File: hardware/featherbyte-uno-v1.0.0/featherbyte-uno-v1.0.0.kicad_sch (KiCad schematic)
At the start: 35 parts, among them J1 Conn_01x08, J2 Conn_01x10, J3 Conn_01x06, J4 Conn_01x08, J5 USB_C_16P, J7 Screw_Terminal_01x02, J8 USB_C_Receptacle_16P, U1 CH32V203CxT6, U4 AMS1117-3.3, U5 USBLC6-2P6, U6 USBLC6-2P6, Y1 8M, Y3 32.768K

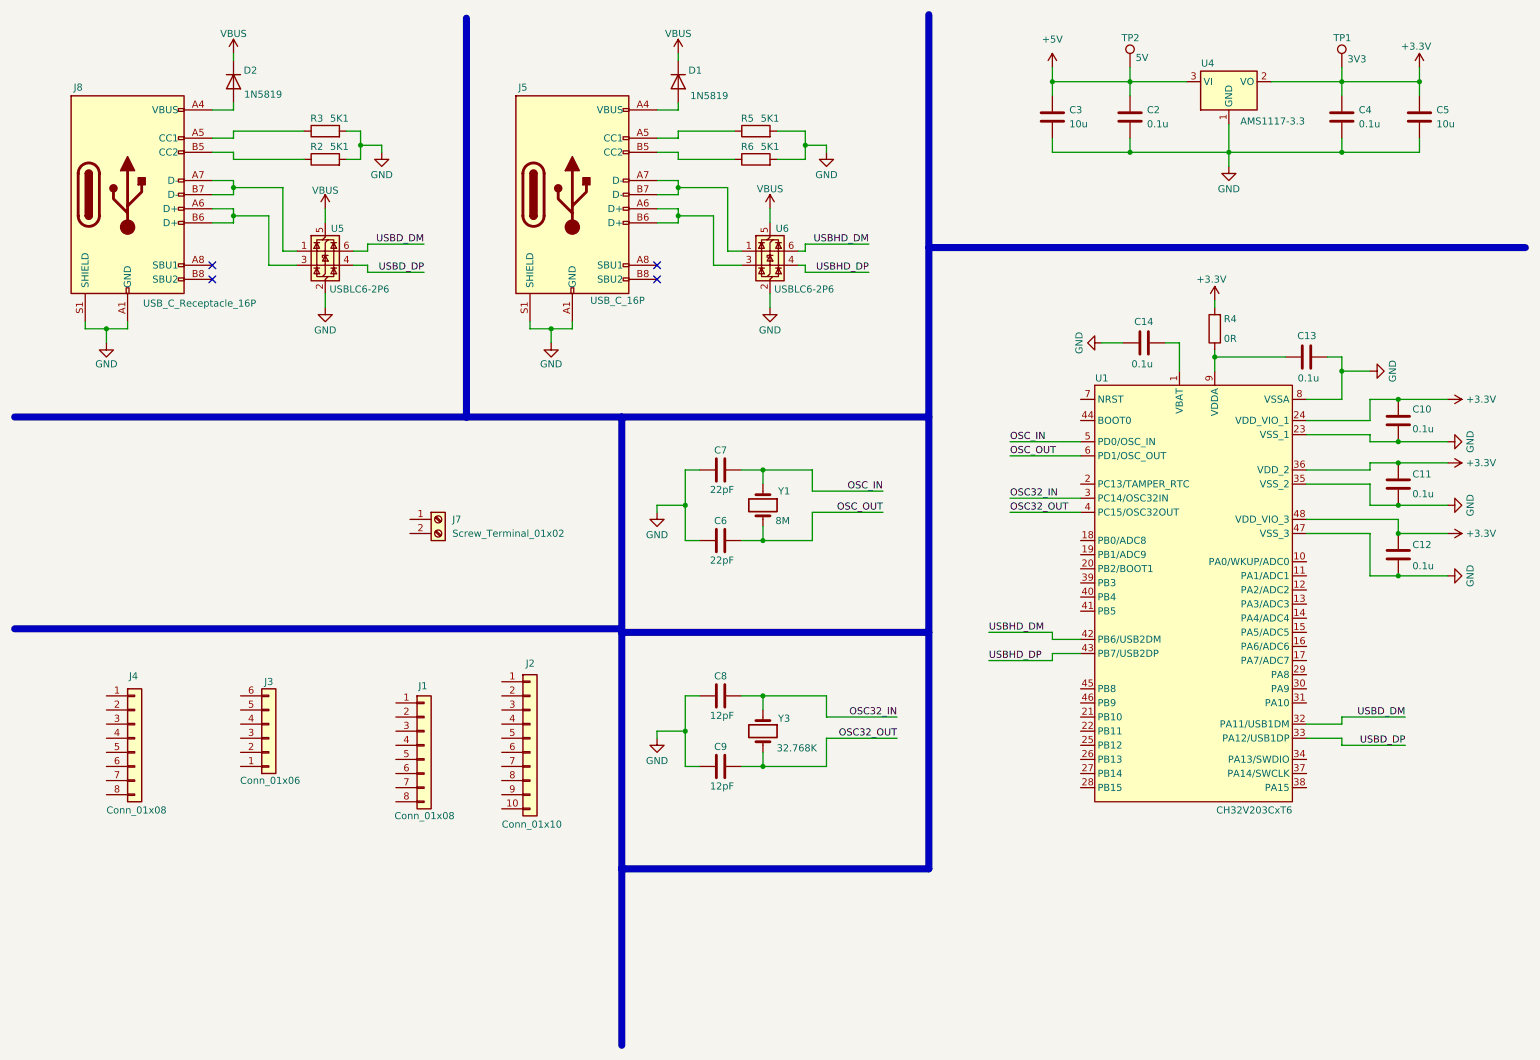
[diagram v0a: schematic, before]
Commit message: canbus, and programing circuitry added
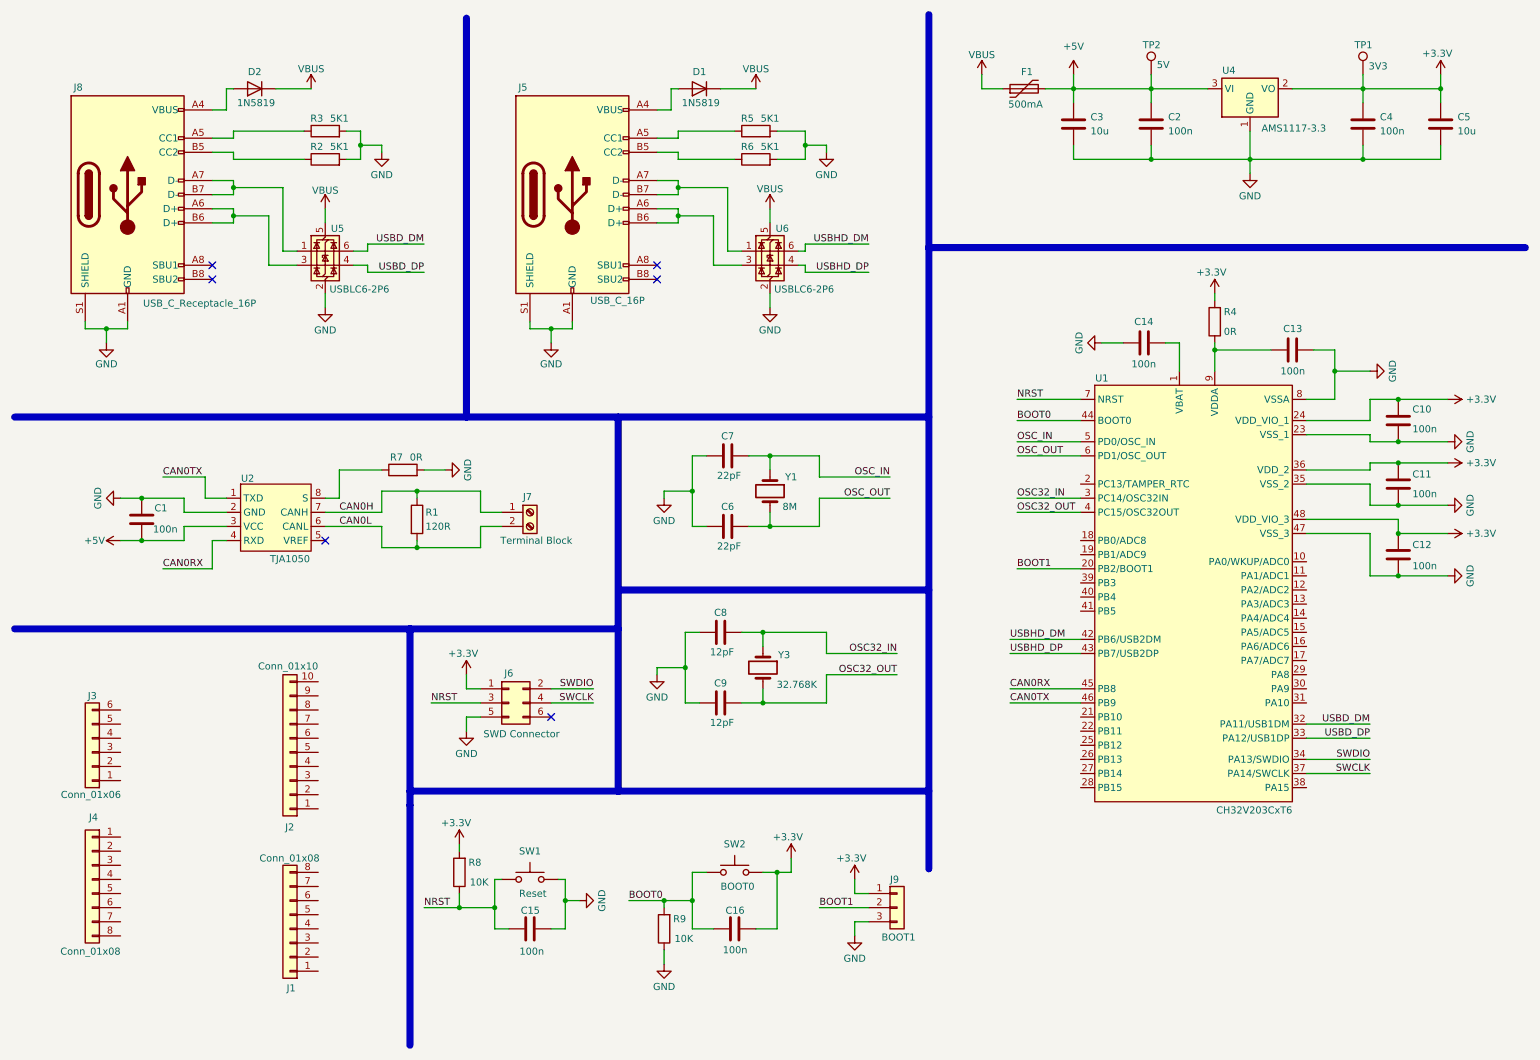
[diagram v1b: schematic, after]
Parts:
- added C1, C15, C16: 100n, symbol Device:C
- added F1: 500mA, symbol Device:Polyfuse
- added J6: SWD Connector, symbol Connector_Generic:Conn_02x03_Odd_Even
- added J9: BOOT1, symbol Connector_Generic:Conn_01x03
- added R1: 120R, symbol Device:R
- added R7: 0R, symbol Device:R
- added R8, R9: 10K, symbol Device:R
- added SW1: Reset, symbol Switch:SW_Push
- added SW2: BOOT0, symbol Switch:SW_Push
- added U2: TJA1050, symbol TJA1050:TJA1050
- C10, C11, C12, C13, C14, C2, C4: value 0.1u -> 100n
- J7: value Screw_Terminal_01x02 -> Terminal Block
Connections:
- net +3.3V: now also C16.2, J6.1 (Pin_1), J9.1 (Pin_1), R8.2, SW2.2
- net +5V: now also C1.2, F1.2, U2.3 (VCC)
- net GND: now also C1.1, C15.2, J6.5 (Pin_5), J9.3 (Pin_3), R7.2, R9.1, SW1.2, U2.2 (GND)
- net VBUS: now also F1.1
- net BOOT1: now reaches U1.20 (PB2/BOOT1)
- net BOOT1: now also J9.2 (Pin_2)
- net SWDIO: now reaches U1.34 (PA13/SWDIO)
- net SWDIO: now also J6.2 (Pin_2)
- net SWCLK: now reaches U1.37 (PA14/SWCLK)
- net SWCLK: now also J6.4 (Pin_4)
- net BOOT0: now reaches U1.44 (BOOT0)
- net BOOT0: now also C16.1, R9.2, SW2.1
- net CAN0RX: now reaches U1.45 (PB8)
- net CAN0RX: now also U2.4 (RXD)
- net CAN0TX: now reaches U1.46 (PB9)
- net CAN0TX: now also U2.1 (TXD)
- net NRST: now reaches U1.7 (NRST)
- net NRST: now also C15.1, J6.3 (Pin_3), R8.1, SW1.1
- net CAN0H: now reaches J7.1 (Pin_1)
- net CAN0H: now also R1.1, U2.7 (CANH)
- net CAN0L: now reaches J7.2 (Pin_2)
- net CAN0L: now also R1.2, U2.6 (CANL)
- new net: R7.1, U2.8 (S)
- no-connect marks 4 -> 6
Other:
- moved on the sheet: C13, C2, C3, C4, C5, C6, C7, C8, C9, D2, J1, J2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

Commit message: schematics ready for layout
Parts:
- removed J4: Conn_01x08, symbol Connector_Generic:Conn_01x08
- added C17: 10u, symbol Device:C
- added D3: GREEN, symbol Device:LED
- added D4: YELLOW, symbol Device:LED
- added J10: Conn_01x09, symbol Connector_Generic:Conn_01x09
- added JP1: Jumper, symbol Jumper:SolderJumper_2_Open
- added R10, R11, R12, R15, R16: 0R, symbol Device:R
- added R13, R14: 1K, symbol Device:R
- added SW3: SW_DIP_x04, symbol Switch:SW_DIP_x04
- J5: value USB_C_16P -> USB_C_Receptacle_16P
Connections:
- net +3.3V: now also J10.5 (Pin_5), J10.7 (Pin_7), J10.8 (Pin_8), J10.9 (Pin_9), R10.2, R13.1
- net +5V: now also C17.1, J10.1 (Pin_1), J10.4 (Pin_4)
- net CAN0H: now also JP1.2 (B); no longer R1.1
- net GND: now also J2.4 (Pin_4), C17.2, D3.1 (K), D4.1 (K), J10.2 (Pin_2), J10.3 (Pin_3)
- net NRST: now also J10.6 (Pin_6)
- net VBUS: now also R15.2, R16.2
- net SCL: now reaches J2.1 (Pin_1)
- net SCL: now also U1.21 (PB10), R12.2
- net D8: now reaches J2.10 (Pin_10)
- net D8: now also U1.27 (PB14)
- net SDA: now reaches J2.2 (Pin_2)
- net SDA: now also U1.22 (PB11), R11.2
- net VREF: now reaches J2.3 (Pin_3)
- net VREF: now also C13.1, R4.1, U1.9 (VDDA)
- net D13: now reaches J2.5 (Pin_5)
- net D13: now also U1.39 (PB3)
- net D12: now reaches J2.6 (Pin_6)
- net D12: now also U1.40 (PB4)
- net D11: now reaches J2.7 (Pin_7)
- net D11: now also U1.41 (PB5)
- net D10: now reaches J2.8 (Pin_8)
- net D10: now also U1.38 (PA15)
- net D9: now reaches J2.9 (Pin_9)
- net D9: now also U1.28 (PB15)
- net at J5.A5 (CC1): now also SW3.1, SW3.2; no longer R5.1
- net at J5.B5 (CC2): now also SW3.3, SW3.4; no longer R6.1
- net D0: now reaches J1.1 (Pin_1)
- net D0: now also U1.13 (PA3/ADC3)
- net D1: now reaches J1.2 (Pin_2)
- net D1: now also U1.12 (PA2/ADC2)
- net D2: now reaches J1.3 (Pin_3)
- net D2: now also U1.16 (PA6/ADC6)
- net D3: now reaches J1.4 (Pin_4)
- net D3: now also U1.17 (PA7/ADC7)
- net D4: now reaches J1.5 (Pin_5)
- net D4: now also U1.29 (PA8)
- net D5: now reaches J1.6 (Pin_6)
- net D5: now also U1.30 (PA9)
- net D6: now reaches J1.7 (Pin_7)
- net D6: now also U1.31 (PA10)
- net D7: now reaches J1.8 (Pin_8)
- net D7: now also U1.26 (PB13)
- net A5: now reaches J3.1 (Pin_1)
- net A5: now also U1.19 (PB1/ADC9), R12.1
- net A4: now reaches J3.2 (Pin_2)
- net A4: now also U1.18 (PB0/ADC8), R11.1
- net A3: now reaches J3.3 (Pin_3)
- net A3: now also U1.15 (PA5/ADC5)
- net A2: now reaches J3.4 (Pin_4)
- net A2: now also U1.14 (PA4/ADC4)
- net A1: now reaches J3.5 (Pin_5)
- net A1: now also U1.11 (PA1/ADC1)
- net A0: now reaches J3.6 (Pin_6)
- net A0: now also U1.10 (PA0/WKUP/ADC0)
- net at C14.1, U1.1 (VBAT): now also R10.1
- net LED: now reaches U1.25 (PB12)
- net LED: now also R14.1
- new net: D4.2 (A), R14.2
- new net: JP1.1 (A), R1.1
- new net: D3.2 (A), R13.2
- new net: R15.1, SW3.5
- new net: R6.1, SW3.6
- new net: R5.1, SW3.7
- new net: R16.1, SW3.8
- no-connect marks 6 -> 7
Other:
- moved on the sheet: C1, C13, C14, C16, C2, C3, C4, C5, C6, C7, C8, C9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

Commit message: footprint asignment complete
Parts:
- C1, C10, C11, C12, C13, C14, C15, C16, C2, C4, C6, C7, C8, C9: footprint (none) -> Capacitor_SMD:C_0603_1608Metric
- C17, C3, C5: footprint (none) -> Capacitor_SMD:C_1206_3216Metric
- D1, D2: footprint (none) -> Diode_SMD:D_SOD-123
- D3, D4: footprint (none) -> LED_SMD:LED_0805_2012Metric
- F1: footprint (none) -> Fuse:Fuse_1206_3216Metric
- J1: footprint (none) -> Connector_PinSocket_2.54mm:PinSocket_1x08_P2.54mm_Vertical
- J10: footprint (none) -> Connector_PinSocket_2.54mm:PinSocket_1x09_P2.54mm_Vertical
- J2: footprint (none) -> Connector_PinSocket_2.54mm:PinSocket_1x10_P2.54mm_Vertical
- J3: footprint (none) -> Connector_PinSocket_2.54mm:PinSocket_1x06_P2.54mm_Vertical
- J5, J8: footprint (none) -> Connector_USB:USB_C_Receptacle_HCTL_HC-TYPE-C-16P-01A
- J6: footprint (none) -> Connector_PinHeader_2.54mm:PinHeader_2x03_P2.54mm_Vertical
- J7: footprint (none) -> TerminalBlock:TerminalBlock_MaiXu_MX126-5.0-02P_1x02_P5.00mm
- J9: footprint (none) -> Connector_PinHeader_2.54mm:PinHeader_1x03_P2.54mm_Vertical
- JP1: footprint (none) -> Jumper:SolderJumper-2_P1.3mm_Open_TrianglePad1.0x1.5mm
- R1, R10, R11, R12, R13, R14, R15, R16, R2, R3, R4, R5, R6, R7, R8, R9: footprint (none) -> Resistor_SMD:R_0603_1608Metric
- SW1, SW2: footprint (none) -> Button_Switch_SMD:SW_SPST_CK_RS282G05A3
- SW3: footprint (none) -> Button_Switch_SMD:SW_DIP_SPSTx04_Slide_KingTek_DSHP04TS_W7.62mm_P1.27mm
- TP1, TP2: footprint (none) -> TestPoint:TestPoint_Pad_D1.5mm
- U1: footprint (none) -> Package_QFP:LQFP-48_7x7mm_P0.5mm
- U2: footprint (none) -> Package_SO:SO-8_3.9x4.9mm_P1.27mm
- Y1: footprint (none) -> Crystal:Crystal_SMD_HC49-SD
- Y3: footprint (none) -> Crystal:Crystal_SMD_3215-2Pin_3.2x1.5mm
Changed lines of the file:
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@@
 			)
 		)
-		(property "Footprint" ""
+		(property "Footprint" "Resistor_SMD:R_0603_1608Metric"
 			(at 94.488 165.1 90)
 			(effects
@@
 			)
 		)
-		(property "Footprint" ""
+		(property "Footprint" "Capacitor_SMD:C_0603_1608Metric"
 			(at 262.5852 100.33 0)
 			(effects
@@
 			)
 		)
-		(property "Footprint" ""
+		(property "Footprint" "Crystal:Crystal_SMD_3215-2Pin_3.2x1.5mm"
 			(at 151.13 129.54 0)
 			(effects
@@
 			)
 		)
-		(property "Footprint" ""
+		(property "Footprint" "Resistor_SMD:R_0603_1608Metric"
 			(at 131.318 176.53 90)
 			(effects
@@
 			)
 		)
-		(property "Footprint" ""
+		(property "Footprint" "Connector_PinSocket_2.54mm:PinSocket_1x10_P2.54mm_Vertical"
 			(at 64.77 179.07 0)
 			(effects
@@
 			)
 		)
-		(property "Footprint" ""
+		(property "Footprint" "Capacitor_SMD:C_0603_1608Metric"
 			(at 32.7152 106.68 0)
 			(effects
@@
 			)
 		)
-		(property "Footprint" ""
+		(property "Footprint" "Connector_PinHeader_2.54mm:PinHeader_1x03_P2.54mm_Vertical"
 			(at 171.45 170.18 0)
 			(effects
@@
 			)
 		)
-		(property "Footprint" ""
+		(property "Footprint" "Resistor_SMD:R_0603_1608Metric"
 			(at 69.85 39.878 90)
 			(effects
@@
 			)
 		)
-		(property "Footprint" ""
+		(property "Footprint" "Capacitor_SMD:C_0603_1608Metric"
 			(at 224.4852 35.56 0)
 			(effects
@@
 			)
 		)
-		(property "Footprint" ""
+		(property "Footprint" "Capacitor_SMD:C_1206_3216Metric"
 			(at 272.7452 35.56 0)
 			(effects
@@
 			)
 		)
-		(property "Footprint" ""
+		(property "Footprint" "Diode_SMD:D_SOD-123"
 			(at 57.15 22.86 0)
 			(effects
@@
 			)
 		)
-		(property "Footprint" ""
+		(property "Footprint" "TestPoint:TestPoint_Pad_D1.5mm"
 			(at 228.6 22.86 0)
 			(effects
@@
 			)
 		)
-		(property "Footprint" ""
+		(property "Footprint" "Capacitor_SMD:C_1206_3216Metric"
 			(at 213.0552 35.56 0)
 			(effects
@@
 			)
 		)
-		(property "Footprint" ""
+		(property "Footprint" "Capacitor_SMD:C_0603_1608Metric"
 			(at 139.7 103.8352 0)
 			(effects
@@
 			)
 		)
-		(property "Footprint" ""
+		(property "Footprint" "Resistor_SMD:R_0603_1608Metric"
 			(at 218.948 67.31 90)
 			(effects
@@
 			)
 		)
-		(property "Footprint" ""
+		(property "Footprint" "Capacitor_SMD:C_0603_1608Metric"
 			(at 139.7 136.8552 0)
 			(effects
@@
 			)
 		)
-		(property "Footprint" ""
+		(property "Footprint" "Resistor_SMD:R_0603_1608Metric"
 			(at 29.21 131.318 90)
 			(effects
@@
 			)
 		)
-		(property "Footprint" ""
+		(property "Footprint" "Connector_USB:USB_C_Receptacle_HCTL_HC-TYPE-C-16P-01A"
 			(at 114.3 41.91 0)
 			(effects
@@
 			)
 		)
-		(property "Footprint" ""
+		(property "Footprint" "LED_SMD:LED_0805_2012Metric"
 			(at 64.77 148.59 0)
 			(effects
@@
 			)
 		)
-		(property "Footprint" ""
+		(property "Footprint" "Jumper:SolderJumper-2_P1.3mm_Open_TrianglePad1.0x1.5mm"
 			(at 82.55 100.33 0)
 			(effects
@@
 			)
 		)
-		(property "Footprint" ""
+		(property "Footprint" "Resistor_SMD:R_0603_1608Metric"
 			(at 55.88 150.368 90)
 			(effects
@@
 			)
 		)
-		(property "Footprint" ""
+		(property "Footprint" "Resistor_SMD:R_0603_1608Metric"
 			(at 230.378 67.31 90)
 			(effects
@@
 			)
 		)
-		(property "Footprint" ""
+		(property "Footprint" "Resistor_SMD:R_0603_1608Metric"
 			(at 55.88 137.668 90)
 			(effects
@@
 			)
 		)
-		(property "Footprint" ""
+		(property "Footprint" "Capacitor_SMD:C_0603_1608Metric"
 			(at 139.7 124.1552 0)
 			(effects
@@
 			)
 		)
-		(property "Footprint" ""
+		(property "Footprint" "Capacitor_SMD:C_1206_3216Metric"
 			(at 201.6252 35.56 0)
 			(effects
@@
 			)
 		)
-		(property "Footprint" ""
+		(property "Footprint" "Button_Switch_SMD:SW_DIP_SPSTx04_Slide_KingTek_DSHP04TS_W7.62mm_P1.27mm"
 			(at 146.05 34.29 0)
 			(effects
@@
 			)
 		)
-		(property "Footprint" ""
+		(property "Footprint" "Capacitor_SMD:C_0603_1608Metric"
 			(at 248.92 71.4248 0)
 			(effects
@@
 			)
 		)
-		(property "Footprint" ""
+		(property "Footprint" "Capacitor_SMD:C_0603_1608Metric"
 			(at 262.5852 88.9 0)
 			(effects
@@
 			)
 		)
-		(property "Footprint" ""
+		(property "Footprint" "Crystal:Crystal_SMD_HC49-SD"
 			(at 151.13 96.52 0)
 			(effects
@@
 			)
 		)
-		(property "Footprint" ""
+		(property "Footprint" "Connector_PinHeader_2.54mm:PinHeader_2x03_P2.54mm_Vertical"
 			(at 101.6 134.62 0)
 			(effects
@@
 			)
 		)
-		(property "Footprint" ""
+		(property "Footprint" "Connector_PinSocket_2.54mm:PinSocket_1x09_P2.54mm_Vertical"
 			(at 21.59 154.94 0)
 			(effects
@@
 			)
 		)
-		(property "Footprint" ""
+		(property "Footprint" "Package_SO:SO-8_3.9x4.9mm_P1.27mm"
 			(at 49.53 96.52 0)
 			(effects
@@
 			)
 		)
-		(property "Footprint" ""
+		(property "Footprint" "Resistor_SMD:R_0603_1608Metric"
 			(at 69.85 32.258 90)
 			(effects
@@
 			)
 		)
-		(property "Footprint" ""
+		(property "Footprint" "Button_Switch_SMD:SW_SPST_CK_RS282G05A3"
 			(at 105.41 162.56 0)
 			(effects
@@
 			)
 		)
-		(property "Footprint" ""
+		(property "Footprint" "LED_SMD:LED_0805_2012Metric"
 			(at 64.77 135.89 0)
 			(effects
@@
 			)
 		)
-		(property "Footprint" ""
+		(property "Footprint" "Connector_USB:USB_C_Receptacle_HCTL_HC-TYPE-C-16P-01A"
 			(at 38.1 43.18 0)
 			(effects
@@
 			)
 		)
-		(property "Footprint" ""
+		(property "Footprint" "Resistor_SMD:R_0603_1608Metric"
 			(at 161.29 46.228 90)
 			(effects
@@
 			)
 		)
-		(property "Footprint" ""
+		(property "Footprint" "Resistor_SMD:R_0603_1608Metric"
 			(at 29.21 137.668 90)
 			(effects
@@
 			)
 		)
-		(property "Footprint" ""
+		(property "Footprint" "Fuse:Fuse_1206_3216Metric"
 			(at 198.12 24.13 0)
 			(effects
@@
 			)
 		)
-		(property "Footprint" ""
+		(property "Footprint" "Capacitor_SMD:C_0603_1608Metric"
 			(at 262.5852 113.03 0)
 			(effects
@@
 			)
 		)
-		(property "Footprint" ""
+		(property "Footprint" "Resistor_SMD:R_0603_1608Metric"
 			(at 161.29 23.368 90)
 			(effects
@@
 			)
 		)
-		(property "Footprint" ""
+		(property "Footprint" "Capacitor_SMD:C_0603_1608Metric"
 			(at 109.22 175.5648 0)
 			(effects
@@
 			)
 		)
-		(property "Footprint" ""
+		(property "Footprint" "Resistor_SMD:R_0603_1608Metric"
 			(at 80.772 109.22 90)
 			(effects
@@
 			)
 		)
-		(property "Footprint" ""
+		(property "Footprint" "TestPoint:TestPoint_Pad_D1.5mm"
 			(at 264.16 22.86 0)
 			(effects
@@
 			)
 		)
-		(property "Footprint" ""
+		(property "Footprint" "Resistor_SMD:R_0603_1608Metric"
 			(at 161.29 30.988 90)
 			(effects
@@
 			)
 		)
-		(property "Footprint" ""
+		(property "Footprint" "Button_Switch_SMD:SW_SPST_CK_RS282G05A3"
 			(at 142.24 161.29 0)
 			(effects
@@
 			)
 		)
-		(property "Footprint" ""
+		(property "Footprint" "Connector_PinSocket_2.54mm:PinSocket_1x08_P2.54mm_Vertical"
 			(at 43.18 184.15 0)
 			(effects
@@
 			)
 		)
-		(property "Footprint" ""
+		(property "Footprint" "Connector_PinSocket_2.54mm:PinSocket_1x06_P2.54mm_Vertical"
 			(at 21.59 186.69 0)
 			(effects
@@
 			)
 		)
-		(property "Footprint" ""
+		(property "Footprint" "Capacitor_SMD:C_0603_1608Metric"
 			(at 146.05 174.2948 0)
 			(effects
@@
 			)
 		)
-		(property "Footprint" ""
+		(property "Footprint" "Diode_SMD:D_SOD-123"
 			(at 132.08 22.86 0)
 			(effects
@@
 			)
 		)
-		(property "Footprint" ""
+		(property "Footprint" "Capacitor_SMD:C_0603_1608Metric"
 			(at 139.7 91.1352 0)
 			(effects
@@
 			)
 		)
-		(property "Footprint" ""
+		(property "Footprint" "Package_QFP:LQFP-48_7x7mm_P0.5mm"
 			(at 207.01 78.74 0)
 			(effects
@@
 			)
 		)
-		(property "Footprint" ""
+		(property "Footprint" "Capacitor_SMD:C_0603_1608Metric"
 			(at 198.12 71.4248 0)
 			(effects
@@
 			)
 		)
-		(property "Footprint" ""
+		(property "Footprint" "Capacitor_SMD:C_0603_1608Metric"
 			(at 260.0452 35.56 0)
 			(effects
@@
 			)
 		)
-		(property "Footprint" ""
+		(property "Footprint" "Resistor_SMD:R_0603_1608Metric"
 			(at 72.39 91.948 90)
 			(effects
@@
 			)
 		)
-		(property "Footprint" ""
+		(property "Footprint" "TerminalBlock:TerminalBlock_MaiXu_MX126-5.0-02P_1x02_P5.00mm"
 			(at 101.6 102.87 0)
 			(effects
@@
 			)
 		)
-		(property "Footprint" ""
+		(property "Footprint" "Resistor_SMD:R_0603_1608Metric"
 			(at 161.29 38.608 90)
 			(effects
